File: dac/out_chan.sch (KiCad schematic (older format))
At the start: 22 parts, among them U101 OPA2210, U102 OPA1611

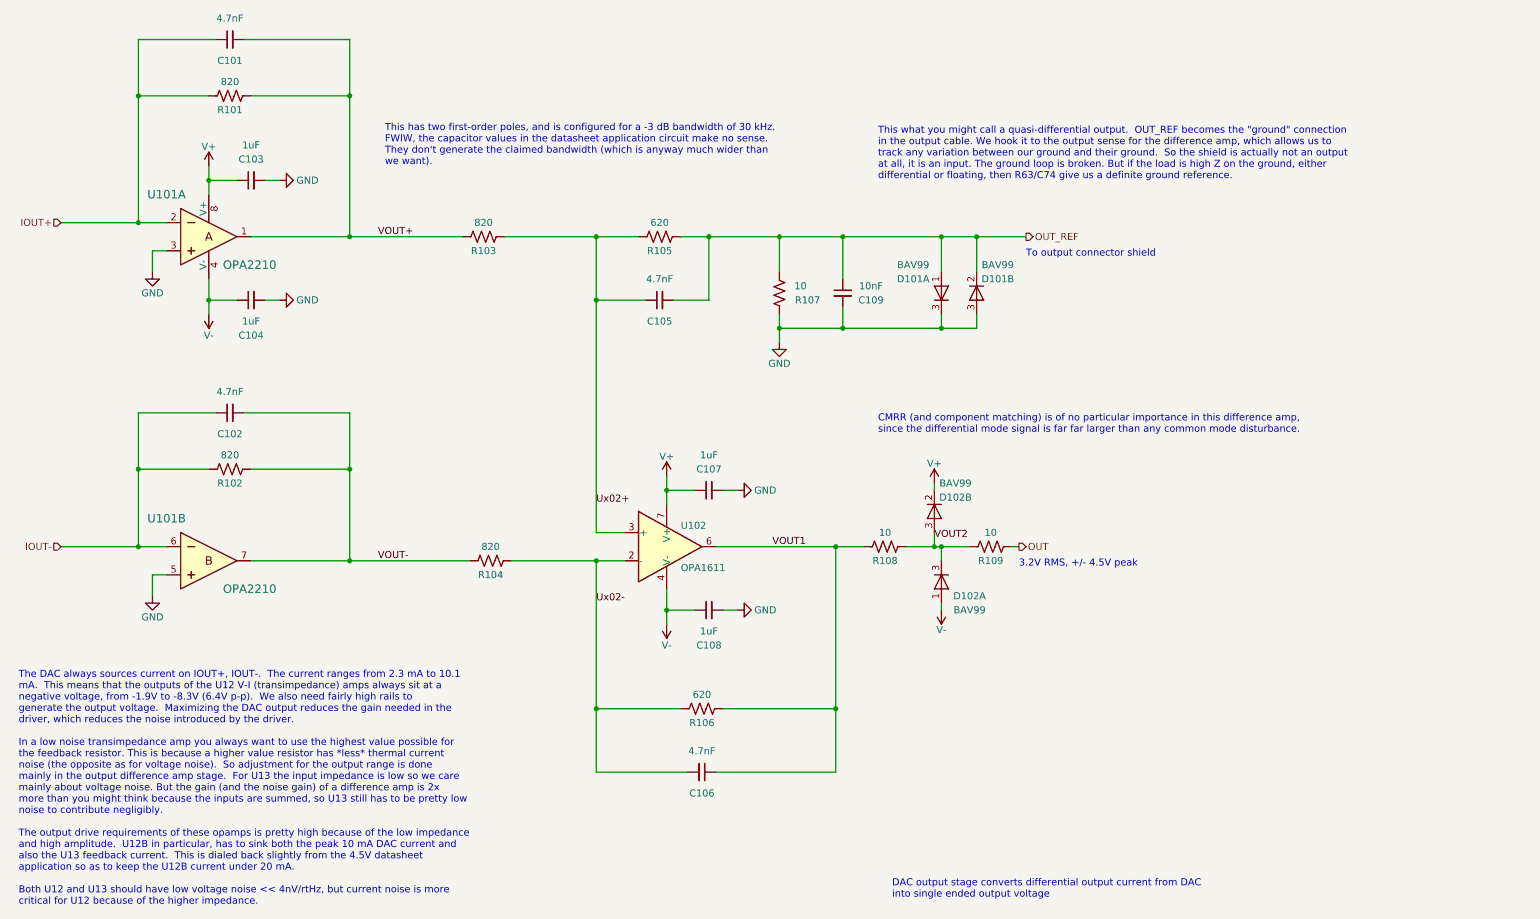
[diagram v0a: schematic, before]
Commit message: DAC board is routed.  I also changed the digital interface to use a buffer (like I did on the input board) so that everything is buffered and we don't have multi-drop nets.
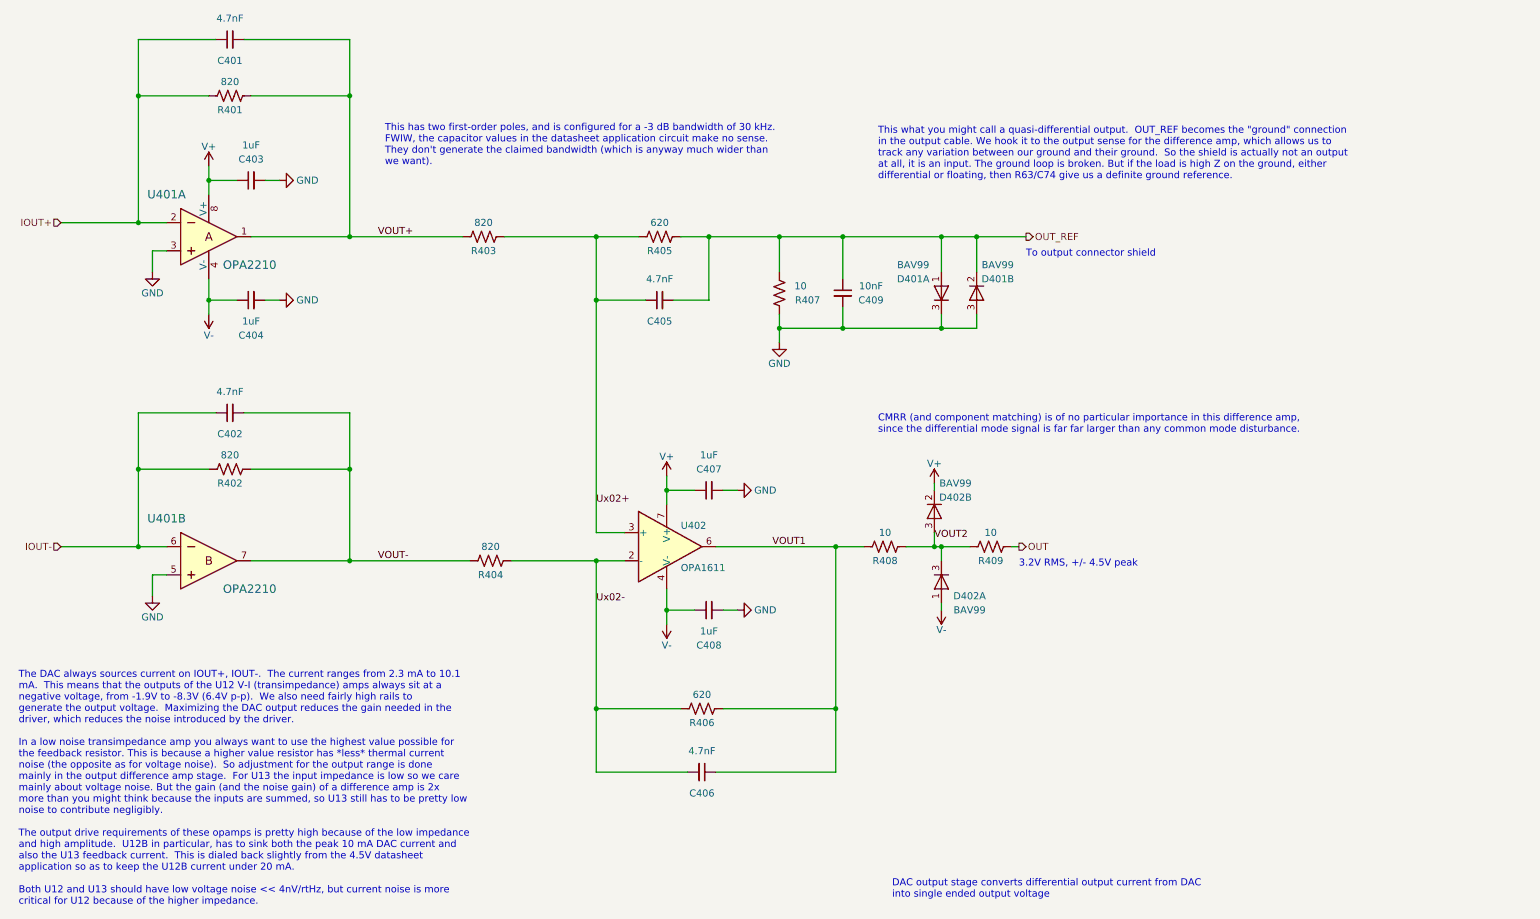
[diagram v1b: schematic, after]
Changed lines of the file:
@@
 $Descr A4 11693 8268
 encoding utf-8
-Sheet 5 11
+Sheet 8 11
 Title ""
 Date ""
@@
 AR Path="/5F8C3863/5F8AE34F/5F81F6F8" Ref="C303"  Part="1"
 AR Path="/5F8C3863/5F8B0DF1/5F81F6F8" Ref="C403"  Part="1"
-F 0 "C103" V 2750 1800 50  0000 C CNN
+F 0 "C403" V 2750 1800 50  0000 C CNN
 F 1 "1uF" V 2850 1800 50  0000 C CNN
 F 2 "Capacitor_SMD:C_0805_2012Metric" H 2600 1800 50  0001 C CNN
@@
 AR Path="/5F8C3863/5F8AE34F/5F810F5B" Ref="U301"  Part="1"
 AR Path="/5F8C3863/5F8B0DF1/5F810F5B" Ref="U401"  Part="1"
-F 0 "U101" H 2000 2500 60  0000 C CNN
+F 0 "U401" H 2000 2500 60  0000 C CNN
 F 1 "OPA2210" H 2400 2000 60  0000 L CNN
 F 2 "Package_SO:SOIC-8_3.9x4.9mm_P1.27mm" H 2500 2400 60  0001 L CNN
@@
 AR Path="/5F8C3863/5F8AE34F/5F8302ED" Ref="C304"  Part="1"
 AR Path="/5F8C3863/5F8B0DF1/5F8302ED" Ref="C404"  Part="1"
-F 0 "C104" V 2350 2650 50  0000 C CNN
+F 0 "C404" V 2350 2650 50  0000 C CNN
 F 1 "1uF" V 2450 2650 50  0000 C CNN
 F 2 "Capacitor_SMD:C_0805_2012Metric" H 2600 2650 50  0001 C CNN
@@
 AR Path="/5F8C3863/5F8AE34F/5F83413B" Ref="R301"  Part="1"
 AR Path="/5F8C3863/5F8B0DF1/5F83413B" Ref="R401"  Part="1"
-F 0 "R101" V 2550 1200 50  0000 C CNN
+F 0 "R401" V 2550 1200 50  0000 C CNN
 F 1 "820" V 2350 1200 50  0000 C CNN
 F 2 "Resistor_SMD:R_0603_1608Metric" V 2490 1190 50  0001 C CNN
@@
 AR Path="/5F8C3863/5F8AE34F/5F8349E3" Ref="C301"  Part="1"
 AR Path="/5F8C3863/5F8B0DF1/5F8349E3" Ref="C401"  Part="1"
-F 0 "C101" V 2300 800 50  0000 C CNN
+F 0 "C401" V 2300 800 50  0000 C CNN
 F 1 "4.7nF" V 2600 800 50  0000 C CNN
 F 2 "Capacitor_THT:C_Rect_L7.2mm_W2.5mm_P5.00mm_FKS2_FKP2_MKS2_MKP2" H 2450 800 50  0001 C CNN
@@
 AR Path="/5F8C3863/5F8AE34F/5F838F2A" Ref="R303"  Part="1"
 AR Path="/5F8C3863/5F8B0DF1/5F838F2A" Ref="R403"  Part="1"
-F 0 "R103" V 4350 2200 50  0000 C CNN
+F 0 "R403" V 4350 2200 50  0000 C CNN
 F 1 "820" V 4150 2200 50  0000 C CNN
 F 2 "Resistor_SMD:R_0603_1608Metric" V 4290 2190 50  0001 C CNN
@@
 AR Path="/5F8C3863/5F8AE34F/5F83984D" Ref="R305"  Part="1"
 AR Path="/5F8C3863/5F8B0DF1/5F83984D" Ref="R405"  Part="1"
-F 0 "R105" V 5600 2200 50  0000 C CNN
+F 0 "R405" V 5600 2200 50  0000 C CNN
 F 1 "620" V 5400 2200 50  0000 C CNN
 F 2 "Resistor_SMD:R_0603_1608Metric" V 5540 2190 50  0001 C CNN
@@
 AR Path="/5F8C3863/5F8AE34F/5F83B3FD" Ref="U302"  Part="1"
 AR Path="/5F8C3863/5F8B0DF1/5F83B3FD" Ref="U402"  Part="1"
-F 0 "U102" H 5650 4550 50  0000 L CNN
+F 0 "U402" H 5650 4550 50  0000 L CNN
 F 1 "OPA1611" H 5650 4250 50  0000 L CNN
 F 2 "Package_SO:SOIC-8_3.9x4.9mm_P1.27mm" H 5600 4425 50  0001 C CNN
@@
 AR Path="/5F8C3863/5F8AE34F/5F8431B2" Ref="C308"  Part="1"
 AR Path="/5F8C3863/5F8B0DF1/5F8431B2" Ref="C408"  Part="1"
-F 0 "C108" V 5600 4850 50  0000 C CNN
+F 0 "C408" V 5600 4850 50  0000 C CNN
 F 1 "1uF" V 5700 4850 50  0000 C CNN
 F 2 "Capacitor_SMD:C_0805_2012Metric" H 5850 4850 50  0001 C CNN
@@
 AR Path="/5F8C3863/5F8AE34F/5F8446C8" Ref="C307"  Part="1"
 AR Path="/5F8C3863/5F8B0DF1/5F8446C8" Ref="C407"  Part="1"
-F 0 "C107" V 6000 4000 50  0000 C CNN
+F 0 "C407" V 6000 4000 50  0000 C CNN
 F 1 "1uF" V 6100 4000 50  0000 C CNN
 F 2 "Capacitor_SMD:C_0805_2012Metric" H 5850 4000 50  0001 C CNN
@@
 AR Path="/5F8C3863/5F8AE34F/5F8490E9" Ref="R304"  Part="1"
 AR Path="/5F8C3863/5F8B0DF1/5F8490E9" Ref="R404"  Part="1"
-F 0 "R104" V 4400 4500 50  0000 C CNN
+F 0 "R404" V 4400 4500 50  0000 C CNN
 F 1 "820" V 4200 4500 50  0000 C CNN
 F 2 "Resistor_SMD:R_0603_1608Metric" V 4340 4490 50  0001 C CNN
@@
 AR Path="/5F8C3863/5F8AE34F/5F8490F2" Ref="R306"  Part="1"
 AR Path="/5F8C3863/5F8B0DF1/5F8490F2" Ref="R406"  Part="1"
-F 0 "R106" V 5700 5550 50  0000 C CNN
+F 0 "R406" V 5700 5550 50  0000 C CNN
 F 1 "620" V 5900 5550 50  0000 C CNN
 F 2 "Resistor_SMD:R_0603_1608Metric" V 5840 5540 50  0001 C CNN
@@
 AR Path="/5F8C3863/5F8AE34F/5F8490F8" Ref="C306"  Part="1"
 AR Path="/5F8C3863/5F8B0DF1/5F8490F8" Ref="C406"  Part="1"
-F 0 "C106" V 5950 6000 50  0000 C CNN
+F 0 "C406" V 5950 6000 50  0000 C CNN
 F 1 "4.7nF" V 5650 6000 50  0000 C CNN
 F 2 "Capacitor_THT:C_Rect_L7.2mm_W2.5mm_P5.00mm_FKS2_FKP2_MKS2_MKP2" H 5800 6000 50  0001 C CNN
@@
 AR Path="/5F8C3863/5F8AE34F/5F85A53F" Ref="U301"  Part="2"
 AR Path="/5F8C3863/5F8B0DF1/5F85A53F" Ref="U401"  Part="2"
-F 0 "U101" H 2000 4800 60  0000 C CNN
+F 0 "U401" H 2000 4800 60  0000 C CNN
 F 1 "OPA2210" H 2400 4300 60  0000 L CNN
 F 2 "Package_SO:SOIC-8_3.9x4.9mm_P1.27mm" H 2500 4700 60  0001 L CNN
@@
 AR Path="/5F8C3863/5F8AE34F/5F85A563" Ref="R302"  Part="1"
 AR Path="/5F8C3863/5F8B0DF1/5F85A563" Ref="R402"  Part="1"
-F 0 "R102" V 2550 3850 50  0000 C CNN
+F 0 "R402" V 2550 3850 50  0000 C CNN
 F 1 "820" V 2350 3850 50  0000 C CNN
 F 2 "Resistor_SMD:R_0603_1608Metric" V 2490 3840 50  0001 C CNN
@@
 AR Path="/5F8C3863/5F8AE34F/5F85A569" Ref="C302"  Part="1"
 AR Path="/5F8C3863/5F8B0DF1/5F85A569" Ref="C402"  Part="1"
-F 0 "C102" V 2300 3450 50  0000 C CNN
+F 0 "C402" V 2300 3450 50  0000 C CNN
 F 1 "4.7nF" V 2600 3450 50  0000 C CNN
 F 2 "Capacitor_THT:C_Rect_L7.2mm_W2.5mm_P5.00mm_FKS2_FKP2_MKS2_MKP2" H 2450 3450 50  0001 C CNN
@@
 AR Path="/5F8C3863/5F8AE34F/5F869EA8" Ref="R308"  Part="1"
 AR Path="/5F8C3863/5F8B0DF1/5F869EA8" Ref="R408"  Part="1"
-F 0 "R108" V 7200 4400 50  0000 C CNN
+F 0 "R408" V 7200 4400 50  0000 C CNN
 F 1 "10" V 7000 4400 50  0000 C CNN
 F 2 "Resistor_SMD:R_0805_2012Metric" V 7140 4390 50  0001 C CNN
@@
 AR Path="/5F8C3863/5F8AE34F/5F83C71D" Ref="C305"  Part="1"
 AR Path="/5F8C3863/5F8B0DF1/5F83C71D" Ref="C405"  Part="1"
-F 0 "C105" V 5350 2650 50  0000 C CNN
+F 0 "C405" V 5350 2650 50  0000 C CNN
 F 1 "4.7nF" V 5650 2650 50  0000 C CNN
 F 2 "Capacitor_THT:C_Rect_L7.2mm_W2.5mm_P5.00mm_FKS2_FKP2_MKS2_MKP2" H 5500 2650 50  0001 C CNN
@@
 AR Path="/5F8C3863/5F8AE34F/5F8A0285" Ref="R307"  Part="1"
 AR Path="/5F8C3863/5F8B0DF1/5F8A0285" Ref="R407"  Part="1"
-F 0 "R107" H 6150 2650 50  0000 C CNN
+F 0 "R407" H 6150 2650 50  0000 C CNN
 F 1 "10" H 6200 2550 50  0000 C CNN
 F 2 "Resistor_SMD:R_0805_2012Metric" V 6390 2590 50  0001 C CNN
@@
 AR Path="/5F8C3863/5F8AE34F/5F8A0AFB" Ref="C309"  Part="1"
 AR Path="/5F8C3863/5F8B0DF1/5F8A0AFB" Ref="C409"  Part="1"
-F 0 "C109" H 7000 2550 50  0000 C CNN
+F 0 "C409" H 7000 2550 50  0000 C CNN
 F 1 "10nF" H 7000 2650 50  0000 C CNN
 F 2 "Capacitor_SMD:C_0805_2012Metric" H 6800 2600 50  0001 C CNN
@@
 AR Path="/5F8C3863/5F8AE34F/5F88E0D6" Ref="D301"  Part="1"
 AR Path="/5F8C3863/5F8B0DF1/5F88E0D6" Ref="D401"  Part="1"
-F 0 "D101" V 7600 2800 50  0000 C CNN
+F 0 "D401" V 7600 2800 50  0000 C CNN
 F 1 "BAV99" V 7700 2800 50  0000 C CNN
 F 2 "Package_TO_SOT_SMD:SOT-23" H 7500 2450 50  0001 C CNN
@@
 AR Path="/5F8C3863/5F8AE34F/5F88E0E1" Ref="D301"  Part="2"
 AR Path="/5F8C3863/5F8B0DF1/5F88E0E1" Ref="D401"  Part="2"
-F 0 "D101" V 7650 2750 50  0000 C CNN
+F 0 "D401" V 7650 2750 50  0000 C CNN
 F 1 "BAV99" V 7550 2750 50  0000 C CNN
 F 2 "Package_TO_SOT_SMD:SOT-23" H 7750 2450 50  0001 C CNN
@@
 AR Path="/5F8C3863/5F8AE34F/5F8AA1D2" Ref="D302"  Part="1"
 AR Path="/5F8C3863/5F8B0DF1/5F8AA1D2" Ref="D402"  Part="1"
-F 0 "D102" V 7600 4850 50  0000 C CNN
+F 0 "D402" V 7600 4850 50  0000 C CNN
 F 1 "BAV99" V 7700 4850 50  0000 C CNN
 F 2 "Package_TO_SOT_SMD:SOT-23" H 7500 4500 50  0001 C CNN
@@
 AR Path="/5F8C3863/5F8AE34F/5F8AA1DD" Ref="D302"  Part="2"
 AR Path="/5F8C3863/5F8B0DF1/5F8AA1DD" Ref="D402"  Part="2"
-F 0 "D102" V 7350 4300 50  0000 C CNN
+F 0 "D402" V 7350 4300 50  0000 C CNN
 F 1 "BAV99" V 7250 4300 50  0000 C CNN
 F 2 "Package_TO_SOT_SMD:SOT-23" H 7450 4000 50  0001 C CNN
@@
 AR Path="/5F8C3863/5F8AE34F/5F8BFA36" Ref="R309"  Part="1"
 AR Path="/5F8C3863/5F8B0DF1/5F8BFA36" Ref="R409"  Part="1"
-F 0 "R109" V 7950 4400 50  0000 C CNN
+F 0 "R409" V 7950 4400 50  0000 C CNN
 F 1 "10" V 7750 4400 50  0000 C CNN
 F 2 "Resistor_SMD:R_0805_2012Metric" V 7890 4390 50  0001 C CNN

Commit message: Everything seems ready to go for the DAC board.  Made my BOM and checked it twice. Checked footprints of new components and fixed J5, R7-R10.
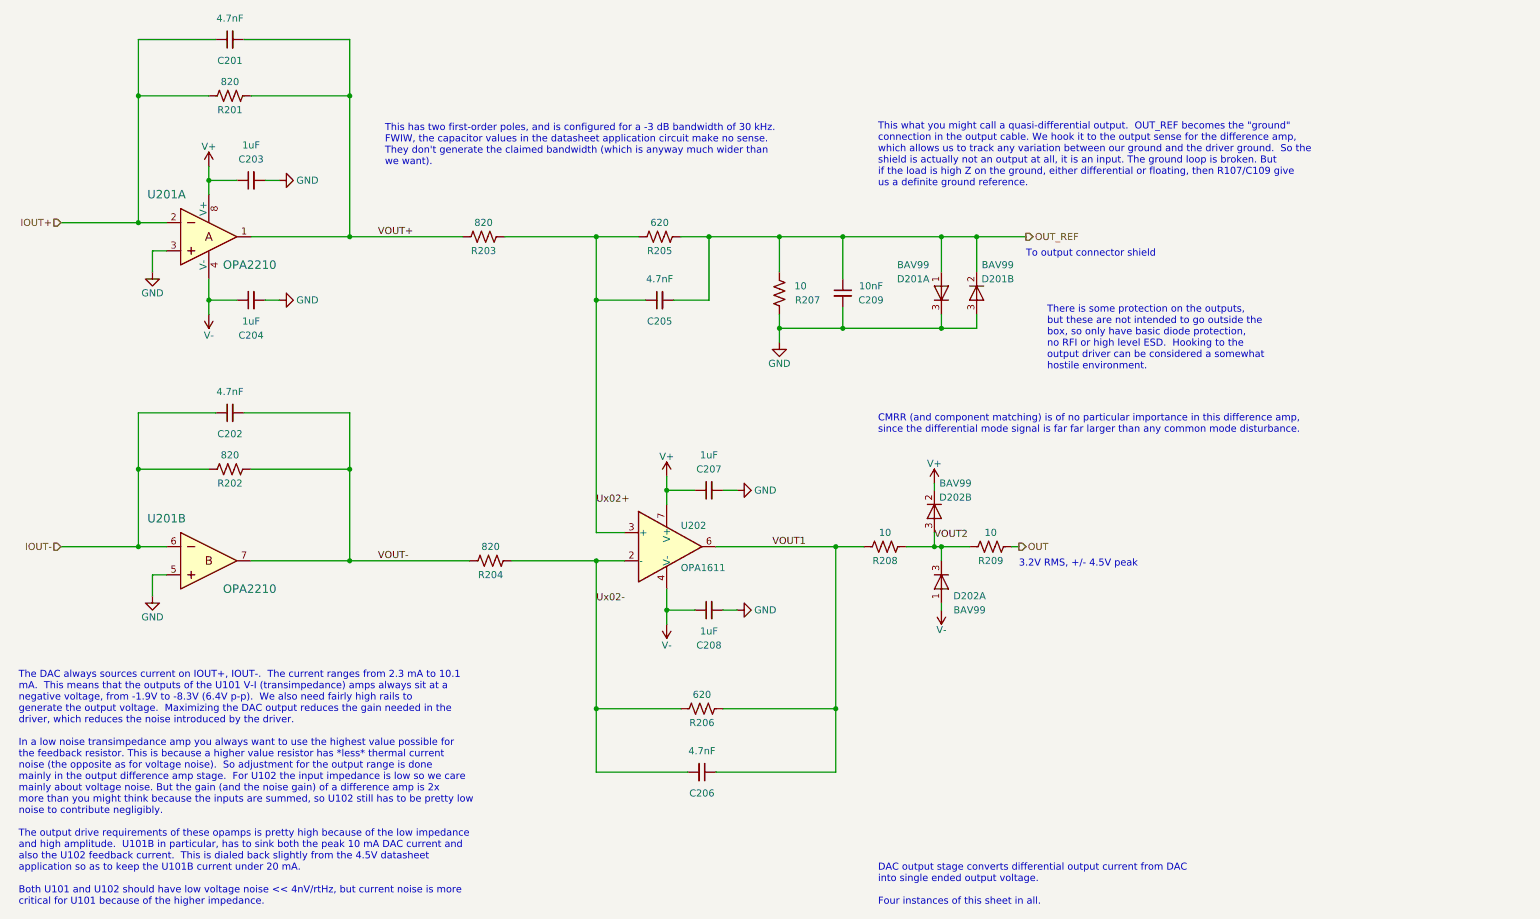
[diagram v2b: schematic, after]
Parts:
- C101, C102, C105, C106: DK line (none) -> D.3
- C103, C104, C107, C108: DK line 27 -> I.27
- C109: DK line (none) -> I.14
- D101, D102: DK line (none) -> D.30; Description (none) -> DIODE ARRAY GP 75V 300MA SOT23-3; Digikey (none) -> BAV99-FDICT-ND; MPN (none) -> BAV99-7-F; Manufacturer (none) -> Diodes Incorporated
- D101, D102: DK line 43 -> D.30; Description DIODE ARRAY GP 250V 225MA SOT23 -> DIODE ARRAY GP 75V 300MA SOT23-3; Digikey BAS21SLT1GOSCT-ND -> BAV99-FDICT-ND; MPN BAS21SLT1G -> BAV99-7-F; Manufacturer ON Semiconductor -> Diodes Incorporated
- R101, R102, R103, R104: DK line (none) -> D.34; Description (none) -> RES SMD 820 OHM 1% 1/8W 0603; Digikey (none) -> 749-1683-1-ND; MPN (none) -> MCT06030C8200FP500; Manufacturer (none) -> Vishay Beyschlag/Draloric/BC Components
- R105, R106: DK line (none) -> D.35; Description (none) -> RES 620 OHM 1% 1/8W 0603; Digikey (none) -> 749-1752-1-ND; MPN (none) -> MCT06030C6200FP500; Manufacturer (none) -> Vishay Beyschlag/Draloric/BC Components
- R107, R108, R109: DK line (none) -> I.52
- U101: DK line (none) -> D.1; Digikey (none) -> 296-OPA2210IDGKRCT-ND; MPN (none) -> OPA2210IDGKR; Manufacturer (none) -> Texas Instruments
- U102: DK line (none) -> D.2; Description (none) -> IC AUDIO 1 CIRCUIT 8SOIC; Digikey (none) -> 296-47811-1-ND; MPN (none) -> OPA1611AIDR; Manufacturer (none) -> Texas Instruments
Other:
- note added: "DAC output stage converts differential output current from DAC\ninto single ended output voltage.\n\nFour instances of this sheet in all."
- note added: "The DAC always sources current on IOUT+, IOUT-. The current ranges from 2.3 mA to 10.1\nmA. This means that the outputs of the U101 V-I (transimpedance) amps always sit at a\nnegative voltage, from -1.9V to -8.3V (6.4V p-p). We also need fairly high rails to\ngenerate the output voltage. Maximizing the DAC output reduces the gain needed in the\ndriver, which reduces the noise introduced by the dr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"
- note added: "This what you might call a quasi-differential output. OUT_REF becomes the "ground"\nconnection in the output cable. We hook it to the output sense for the difference amp,\nwhich allows us to track any variation between our ground and the driver ground. So the\nshield is actually not an output at all, it is an input. The ground loop is broken. But\nif the load is high Z on the ground, either diffe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"
- note added: "\nThere is some protection on the outputs,\nbut these are not intended to go outside the\nbox, so only have basic diode protection,\nno RFI or high level ESD. Hooking to the\noutput driver can be considered a somewhat\nhostile environment."
- note removed: "DAC output stage converts differential output current from DAC\ninto single ended output voltage"
- note removed: "The DAC always sources current on IOUT+, IOUT-. The current ranges from 2.3 mA to 10.1\nmA. This means that the outputs of the U12 V-I (transimpedance) amps always sit at a\nnegative voltage, from -1.9V to -8.3V (6.4V p-p). We also need fairly high rails to\ngenerate the output voltage. Maximizing the DAC output reduces the gain needed in the\ndriver, which reduces the noise introduced by the dri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"
- note removed: "This what you might call a quasi-differential output. OUT_REF becomes the "ground" connection\nin the output cable. We hook it to the output sense for the difference amp, which allows us to \ntrack any variation between our ground and their ground. So the shield is actually not an output\nat all, it is an input. The ground loop is broken. But if the load is high Z on the ground, either \ndifferen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"
